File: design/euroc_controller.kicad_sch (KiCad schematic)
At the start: 63 parts, among them J1 xt30, J2 jst_sh 4, J4 jst_sh 4, J5 jst_sh 4, J6 SMA, J8 USB_C_Receptacle_USB2.0, J9 jst_sh 4, Q1 MMBT3904, U1 TPSM5601R5, U12 STM32L562CETx, U2 USBLC6-2SC6, U3 LSM6DSO32, U4 MS5611-01BA, U5 SN65HVD232, U6 W25Q128JVS, U7 RFM69W, U8 L86, Y1 48MHz

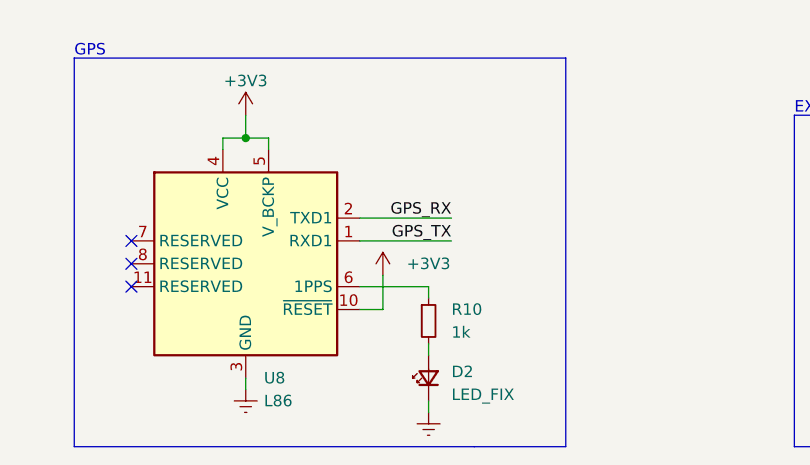
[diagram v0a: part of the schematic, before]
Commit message: align mounting holes
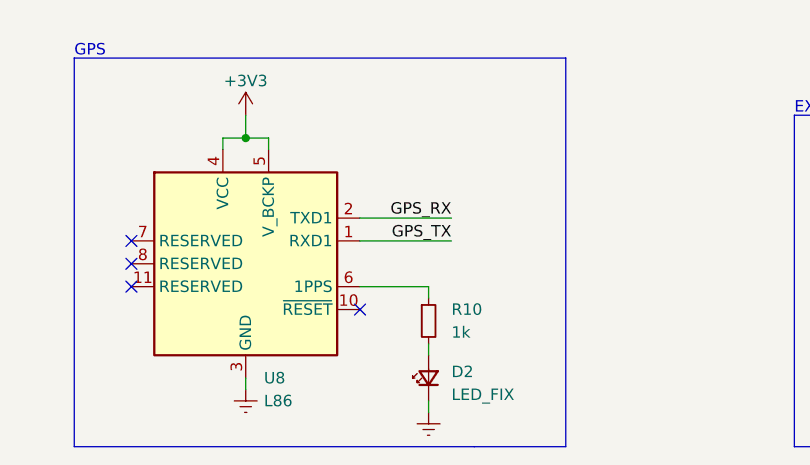
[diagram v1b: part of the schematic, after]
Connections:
- net +3V3: no longer U8.10 (~{RESET})
- no-connect marks 26 -> 27
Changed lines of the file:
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@@
   (no_connect (at 71.12 53.34))
   (no_connect (at 62.23 265.43))
+  (no_connect (at 156.21 262.89))
   (no_connect (at 62.23 260.35))
   (no_connect (at 168.91 97.79))
@@
     (stroke (width 0) (type default))
   )
-  (wire (pts (xy 156.21 262.89) (xy 158.75 262.89))
-    (stroke (width 0) (type default))
-  )
   (wire (pts (xy 154.94 74.93) (xy 168.91 74.93))
     (stroke (width 0) (type default))
@@
     (stroke (width 0) (type default))
   )
-  (wire (pts (xy 158.75 262.89) (xy 158.75 259.08))
-    (stroke (width 0) (type default))
-  )
   (wire (pts (xy 199.39 102.87) (xy 212.09 102.87))
     (stroke (width 0) (type default))
@@
         )
       )
-    )
-  )
-  (symbol (lib_name "+3V3_17") (lib_id "power:+3V3") (at 158.75 259.08 0) (unit 1)
-    (in_bom yes) (on_board yes) (dnp no)
-    (property "Reference" "#PWR052" (at 158.75 262.89 0)
-      (effects (font (size 1.27 1.27)) hide)
-    )
-    (property "Value" "+3V3" (at 163.83 257.81 0)
-      (effects (font (size 1.27 1.27)))
-    )
-    (property "Footprint" "" (at 158.75 259.08 0)
-      (effects (font (size 1.27 1.27)) hide)
-    )
-    (property "Datasheet" "" (at 158.75 259.08 0)
-      (effects (font (size 1.27 1.27)) hide)
-    )
-    (pin "1")
-    (instances
-      (project "euroc_controller"
-        (path "/14304acd-da5a-4fe2-9970-30001d32799f"
-          (reference "#PWR052") (unit 1)
-        )
-      )

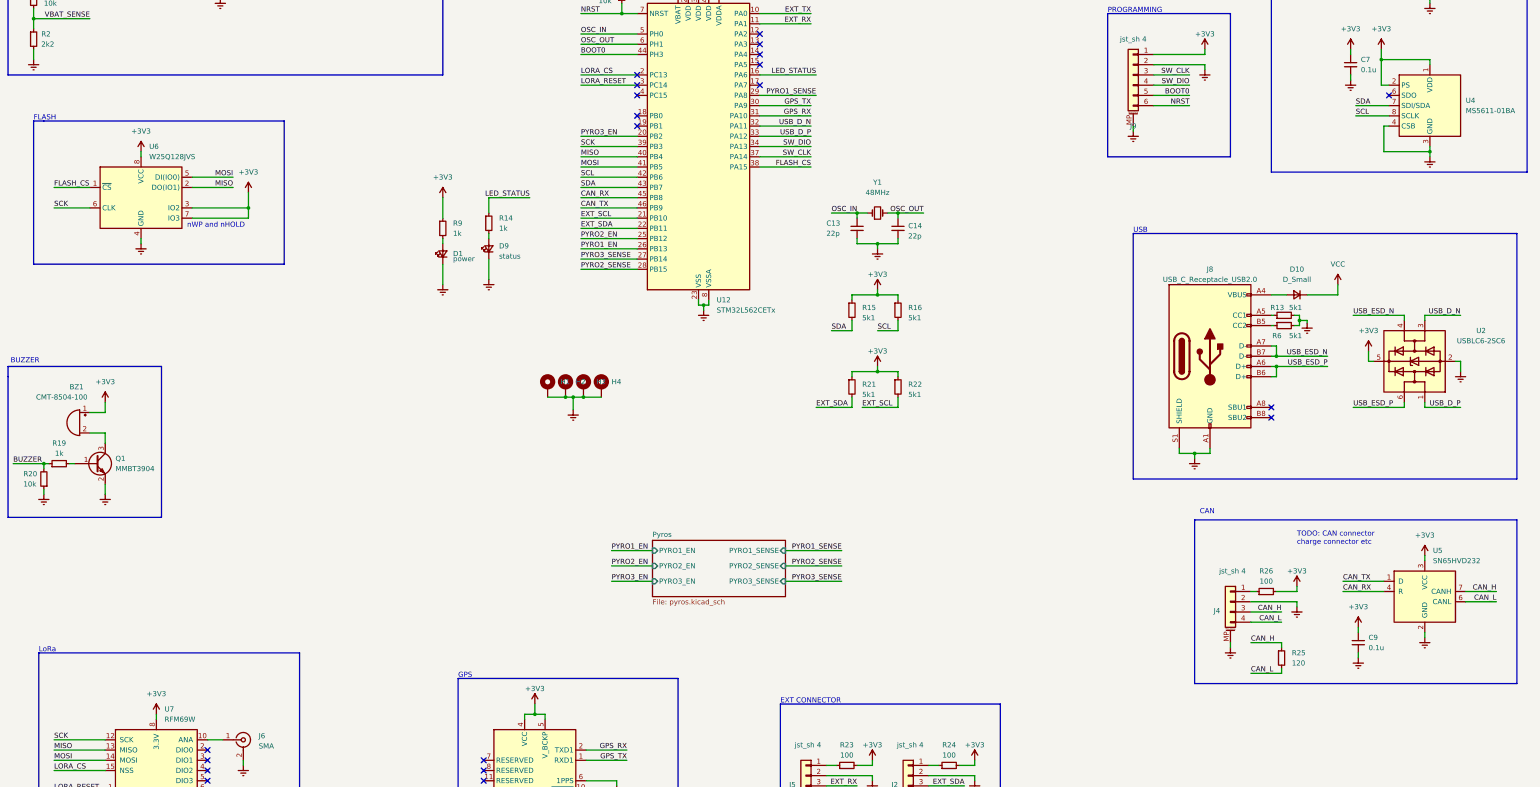
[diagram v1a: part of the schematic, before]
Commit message: use real clock, fix esd vbus
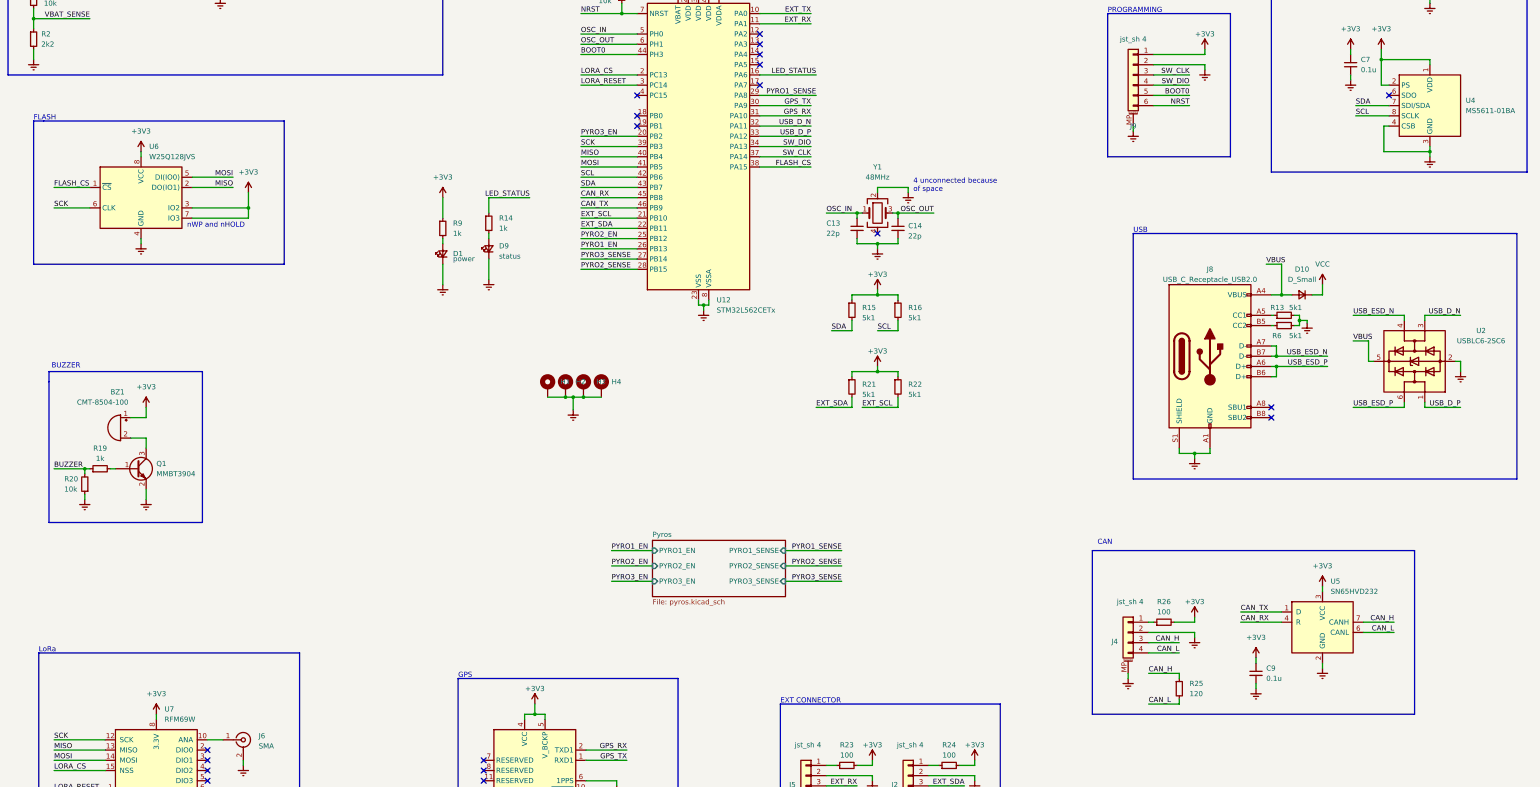
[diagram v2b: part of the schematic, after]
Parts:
- removed Y1: 48MHz, Crystal:Crystal_SMD_2012-2Pin_2.0x1.2mm_HandSoldering, symbol Device:Crystal_Small
- added Y1: 48MHz, Crystal:Crystal_SMD_2016-4Pin_2.0x1.6mm, symbol Device:Crystal_GND24
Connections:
- net +3V3: no longer U2.5 (VBUS)
- net Earth: now also Y1.2
- net OSC_IN: now also Y1.1
- net OSC_OUT: now also Y1.3
- net VBUS: now reaches D10.2 (A), J8.A4 (VBUS), J8.A9 (VBUS), J8.B4 (VBUS), J8.B9 (VBUS)
- net VBUS: now also U2.5 (VBUS)
- no-connect marks 27 -> 26
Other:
- note added: "4 unconnected because of space"
- note removed: "TODO: CAN connector charge connector etc"
- moved on the sheet: BZ1, C9, D10, J4, Q1, R19, R20, R25, R26, U5

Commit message: update ioc, add logo
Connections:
- net BUZZER: now also U12.13 (PA3)
- no-connect marks 26 -> 25
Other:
- moved on the sheet: J9
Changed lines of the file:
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@@
   (no_connect (at 71.12 48.26))
   (no_connect (at 355.6 90.17))
-  (no_connect (at 199.39 77.47))
   (wire (pts (xy 154.94 87.63) (xy 168.91 87.63))
     (stroke (width 0) (type default))
@@
     (stroke (width 0) (type default))
   )
-  (polyline (pts (xy 285.75 69.85) (xy 316.23 69.85))
+  (polyline (pts (xy 285.75 24.13) (xy 316.23 24.13))
     (stroke (width 0) (type default))
   )
@@
     (stroke (width 0) (type default))
   )
-  (wire (pts (xy 297.18 85.09) (xy 306.07 85.09))
+  (wire (pts (xy 297.18 39.37) (xy 306.07 39.37))
     (stroke (width 0) (type default))
   )
-  (polyline (pts (xy 285.75 69.85) (xy 285.75 105.41))
+  (polyline (pts (xy 285.75 24.13) (xy 285.75 59.69))
     (stroke (width 0) (type default))
   )
@@
     (stroke (width 0) (type default))
   )
-  (wire (pts (xy 297.18 90.17) (xy 306.07 90.17))
+  (wire (pts (xy 297.18 44.45) (xy 306.07 44.45))
     (stroke (width 0) (type default))
   )
@@
     (stroke (width 0) (type default))
   )
-  (wire (pts (xy 292.1 97.79) (xy 292.1 99.06))
+  (wire (pts (xy 292.1 52.07) (xy 292.1 53.34))
     (stroke (width 0) (type default))
   )
@@
     (stroke (width 0) (type default))
   )
-  (wire (pts (xy 297.18 92.71) (xy 306.07 92.71))
+  (wire (pts (xy 297.18 46.99) (xy 306.07 46.99))
     (stroke (width 0) (type default))
   )
@@
     (stroke (width 0) (type default))
   )
+  (wire (pts (xy 199.39 77.47) (xy 213.36 77.47))
+    (stroke (width 0) (type default))
+  )
   (wire (pts (xy 199.39 69.85) (xy 212.09 69.85))
     (stroke (width 0) (type default))
@@
     (stroke (width 0) (type default))
   )
-  (wire (pts (xy 297.18 82.55) (xy 309.88 82.55))
+  (wire (pts (xy 297.18 36.83) (xy 309.88 36.83))
     (stroke (width 0) (type default))
   )
@@
     (stroke (width 0) (type default))
   )
-  (wire (pts (xy 297.18 80.01) (xy 309.88 80.01))
+  (wire (pts (xy 297.18 34.29) (xy 309.88 34.29))
     (stroke (width 0) (type default))
   )
@@
     (stroke (width 0) (type default))
   )
-  (polyline (pts (xy 316.23 69.85) (xy 316.23 105.41))
+  (polyline (pts (xy 316.23 24.13) (xy 316.23 59.69))
     (stroke (width 0) (type default))
   )
@@
     (stroke (width 0) (type default))
   )
-  (polyline (pts (xy 316.23 105.41) (xy 285.75 105.41))
+  (polyline (pts (xy 316.23 59.69) (xy 285.75 59.69))
     (stroke (width 0) (type default))
   )
@@
     (stroke (width 0) (type default))
   )
-  (wire (pts (xy 309.88 82.55) (xy 309.88 83.82))
+  (wire (pts (xy 309.88 36.83) (xy 309.88 38.1))
     (stroke (width 0) (type default))
   )
@@
     (stroke (width 0) (type default))
   )
-  (wire (pts (xy 309.88 78.74) (xy 309.88 80.01))
+  (wire (pts (xy 309.88 33.02) (xy 309.88 34.29))
     (stroke (width 0) (type default))
   )
@@
     (stroke (width 0) (type default))
   )
-  (wire (pts (xy 297.18 87.63) (xy 306.07 87.63))
+  (wire (pts (xy 297.18 41.91) (xy 306.07 41.91))
     (stroke (width 0) (type default))
   )
@@
     (effects (font (size 1.27 1.27)) (justify left bottom))
   )
-  (text "PROGRAMMING" (at 285.75 69.85 0)
+  (text "PROGRAMMING" (at 285.75 24.13 0)
     (effects (font (size 1.27 1.27)) (justify left bottom))
   )
@@
     (effects (font (size 1.27 1.27)) (justify right bottom))
   )
-  (label "NRST" (at 306.07 92.71 180) (fields_autoplaced)
+  (label "NRST" (at 306.07 46.99 180) (fields_autoplaced)
     (effects (font (size 1.27 1.27)) (justify right bottom))
   )
@@
     (effects (font (size 1.27 1.27)) (justify left bottom))
   )
+  (label "BUZZER" (at 213.36 77.47 180) (fields_autoplaced)
+    (effects (font (size 1.27 1.27)) (justify right bottom))
+  )
   (label "SW_DIO" (at 212.09 102.87 180) (fields_autoplaced)
     (effects (font (size 1.27 1.27)) (justify right bottom))
@@
     (effects (font (size 1.27 1.27)) (justify left bottom))
   )
-  (label "SW_CLK" (at 306.07 85.09 180) (fields_autoplaced)
+  (label "SW_CLK" (at 306.07 39.37 180) (fields_autoplaced)
     (effects (font (size 1.27 1.27)) (justify right bottom))
   )
@@
     (effects (font (size 1.27 1.27)) (justify left bottom))
   )
-  (label "SW_DIO" (at 306.07 87.63 180) (fields_autoplaced)
+  (label "SW_DIO" (at 306.07 41.91 180) (fields_autoplaced)
     (effects (font (size 1.27 1.27)) (justify right bottom))
   )
@@
     (effects (font (size 1.27 1.27)) (justify left bottom))
   )
-  (label "BOOT0" (at 306.07 90.17 180) (fields_autoplaced)
+  (label "BOOT0" (at 306.07 44.45 180) (fields_autoplaced)
     (effects (font (size 1.27 1.27)) (justify right bottom))
   )
@@
     )
   )
-  (symbol (lib_name "Earth_21") (lib_id "power:Earth") (at 292.1 99.06 0) (unit 1)
+  (symbol (lib_name "Earth_21") (lib_id "power:Earth") (at 292.1 53.34 0) (unit 1)
     (in_bom yes) (on_board yes) (dnp no) (fields_autoplaced)
-    (property "Reference" "#PWR049" (at 292.1 105.41 0)
+    (property "Reference" "#PWR049" (at 292.1 59.69 0)
       (effects (font (size 1.27 1.27)) hide)
     )
-    (property "Value" "Earth" (at 292.1 102.87 0)
+    (property "Value" "Earth" (at 292.1 57.15 0)
       (effects (font (size 1.27 1.27)) hide)
     )
-    (property "Footprint" "" (at 292.1 99.06 0)
+    (property "Footprint" "" (at 292.1 53.34 0)
       (effects (font (size 1.27 1.27)) hide)
     )
-    (property "Datasheet" "~" (at 292.1 99.06 0)
+    (property "Datasheet" "~" (at 292.1 53.34 0)
       (effects (font (size 1.27 1.27)) hide)
     )
@@
     )
   )
-  (symbol (lib_id "Connector_Generic_MountingPin:Conn_01x06_MountingPin") (at 292.1 85.09 0) (mirror y) (unit 1)
+  (symbol (lib_id "Connector_Generic_MountingPin:Conn_01x06_MountingPin") (at 292.1 39.37 0) (mirror y) (unit 1)
     (in_bom yes) (on_board yes) (dnp no)
-    (property "Reference" "J9" (at 292.1 97.79 0)
+    (property "Reference" "J9" (at 292.1 52.07 0)
       (effects (font (size 1.27 1.27)))
     )
-    (property "Value" "jst_sh 4" (at 292.1 76.2 0)
+    (property "Value" "jst_sh 4" (at 292.1 30.48 0)
       (effects (font (size 1.27 1.27)))
     )
-    (property "Footprint" "Connector_JST:JST_SH_SM06B-SRSS-TB_1x06-1MP_P1.00mm_Horizontal" (at 292.1 85.09 0)
+    (property "Footprint" "Connector_JST:JST_SH_SM06B-SRSS-TB_1x06-1MP_P1.00mm_Horizontal" (at 292.1 39.37 0)
       (effects (font (size 1.27 1.27)) hide)
     )
-    (property "Datasheet" "~" (at 292.1 85.09 0)
+    (property "Datasheet" "~" (at 292.1 39.37 0)
       (effects (font (size 1.27 1.27)) hide)
     )
@@
     )
   )
-  (symbol (lib_name "+3V3_11") (lib_id "power:+3V3") (at 309.88 78.74 0) (unit 1)
+  (symbol (lib_name "+3V3_11") (lib_id "power:+3V3") (at 309.88 33.02 0) (unit 1)
     (in_bom yes) (on_board yes) (dnp no) (fields_autoplaced)
-    (property "Reference" "#PWR040" (at 309.88 82.55 0)
+    (property "Reference" "#PWR040" (at 309.88 36.83 0)
       (effects (font (size 1.27 1.27)) hide)
     )
-    (property "Value" "+3V3" (at 309.88 74.93 0)
+    (property "Value" "+3V3" (at 309.88 29.21 0)
       (effects (font (size 1.27 1.27)))
     )
-    (property "Footprint" "" (at 309.88 78.74 0)
+    (property "Footprint" "" (at 309.88 33.02 0)
       (effects (font (size 1.27 1.27)) hide)
     )
-    (property "Datasheet" "" (at 309.88 78.74 0)
+    (property "Datasheet" "" (at 309.88 33.02 0)
       (effects (font (size 1.27 1.27)) hide)
     )
@@
     )
   )
-  (symbol (lib_name "Earth_14") (lib_id "power:Earth") (at 309.88 83.82 0) (unit 1)
+  (symbol (lib_name "Earth_14") (lib_id "power:Earth") (at 309.88 38.1 0) (unit 1)
     (in_bom yes) (on_board yes) (dnp no) (fields_autoplaced)
-    (property "Reference" "#PWR039" (at 309.88 90.17 0)
+    (property "Reference" "#PWR039" (at 309.88 44.45 0)
       (effects (font (size 1.27 1.27)) hide)
     )
-    (property "Value" "Earth" (at 309.88 87.63 0)
+    (property "Value" "Earth" (at 309.88 41.91 0)
       (effects (font (size 1.27 1.27)) hide)
     )
-    (property "Footprint" "" (at 309.88 83.82 0)
+    (property "Footprint" "" (at 309.88 38.1 0)
       (effects (font (size 1.27 1.27)) hide)
     )
-    (property "Datasheet" "~" (at 309.88 83.82 0)
+    (property "Datasheet" "~" (at 309.88 38.1 0)
       (effects (font (size 1.27 1.27)) hide)
     )

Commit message: oof new umc (st32u5)
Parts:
- removed U12: STM32L562CETx, Package_QFP:LQFP-48_7x7mm_P0.5mm, symbol MCU_ST_STM32L5:STM32L562CETx
- added U13: STM32U575CGTx, Package_QFP:LQFP-48_7x7mm_P0.5mm, symbol MCU_ST_STM32U5:STM32U575CGTx
- C12: value 100p -> 4u7
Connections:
- net +3V3: now also U13.1 (VBAT), U13.24 (VDD), U13.36 (VDD), U13.48 (VDD), U13.9 (VDDA); no longer C12.1
- net BOOT0: now also U13.44 (PH3)
- net BUZZER: now also U13.13 (PA3)
- net CAN_RX: now also U13.45 (PB8)
- net CAN_TX: now also U13.46 (PB9)
- net EXT_RX: now also U13.11 (PA1)
- net EXT_SCL: now also U13.21 (PB10)
- net EXT_SDA: now also U13.27 (PB14)
- net EXT_TX: now also U13.10 (PA0)
- net Earth: now also C12.1, U13.23 (VSS), U13.35 (VSS), U13.47 (VSS), U13.8 (VSSA); no longer C12.2
- net FLASH_CS: now also U13.38 (PA15)
- net GPS_RX: now also U13.31 (PA10)
- net GPS_TX: now also U13.30 (PA9)
- net LED_STATUS: now also U13.16 (PA6)
- net LORA_CS: now also U13.2 (PC13)
- net LORA_RESET: now also U13.3 (PC14)
- net MISO: now also U13.40 (PB4)
- net MOSI: now also U13.41 (PB5)
- net NRST: now also U13.7 (NRST)
- net OSC_IN: now also U13.5 (PH0)
- net OSC_OUT: now also U13.6 (PH1)
- net PYRO1_EN: now also U13.26 (PB13)
- net PYRO1_SENSE: now also U13.29 (PA8)
- net PYRO2_EN: now also U13.25 (PB12)
- net PYRO2_SENSE: now also U13.28 (PB15)
- net PYRO3_EN: now also U13.20 (PB2)
- net PYRO3_SENSE: now also U13.12 (PA2)
- net SCK: now also U13.39 (PB3)
- net SCL: now also U13.42 (PB6)
- net SDA: now also U13.43 (PB7)
- net SW_CLK: now also U13.37 (PA14)
- net SW_DIO: now also U13.34 (PA13)
- net USB_D_N: now also U13.32 (PA11)
- net USB_D_P: now also U13.33 (PA12)
- new net: C12.2, U13.22 (VCAP)
- no-connect marks 25 -> 31

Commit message: fix new umc...
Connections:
- no-connect marks 31 -> 24
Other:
- note added: "stm32u58xxxitxxxsomething is also fine"
- moved on the sheet: C12, R18, U13
